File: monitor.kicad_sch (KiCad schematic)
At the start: 6 parts, among them U20 ADS8568SPM

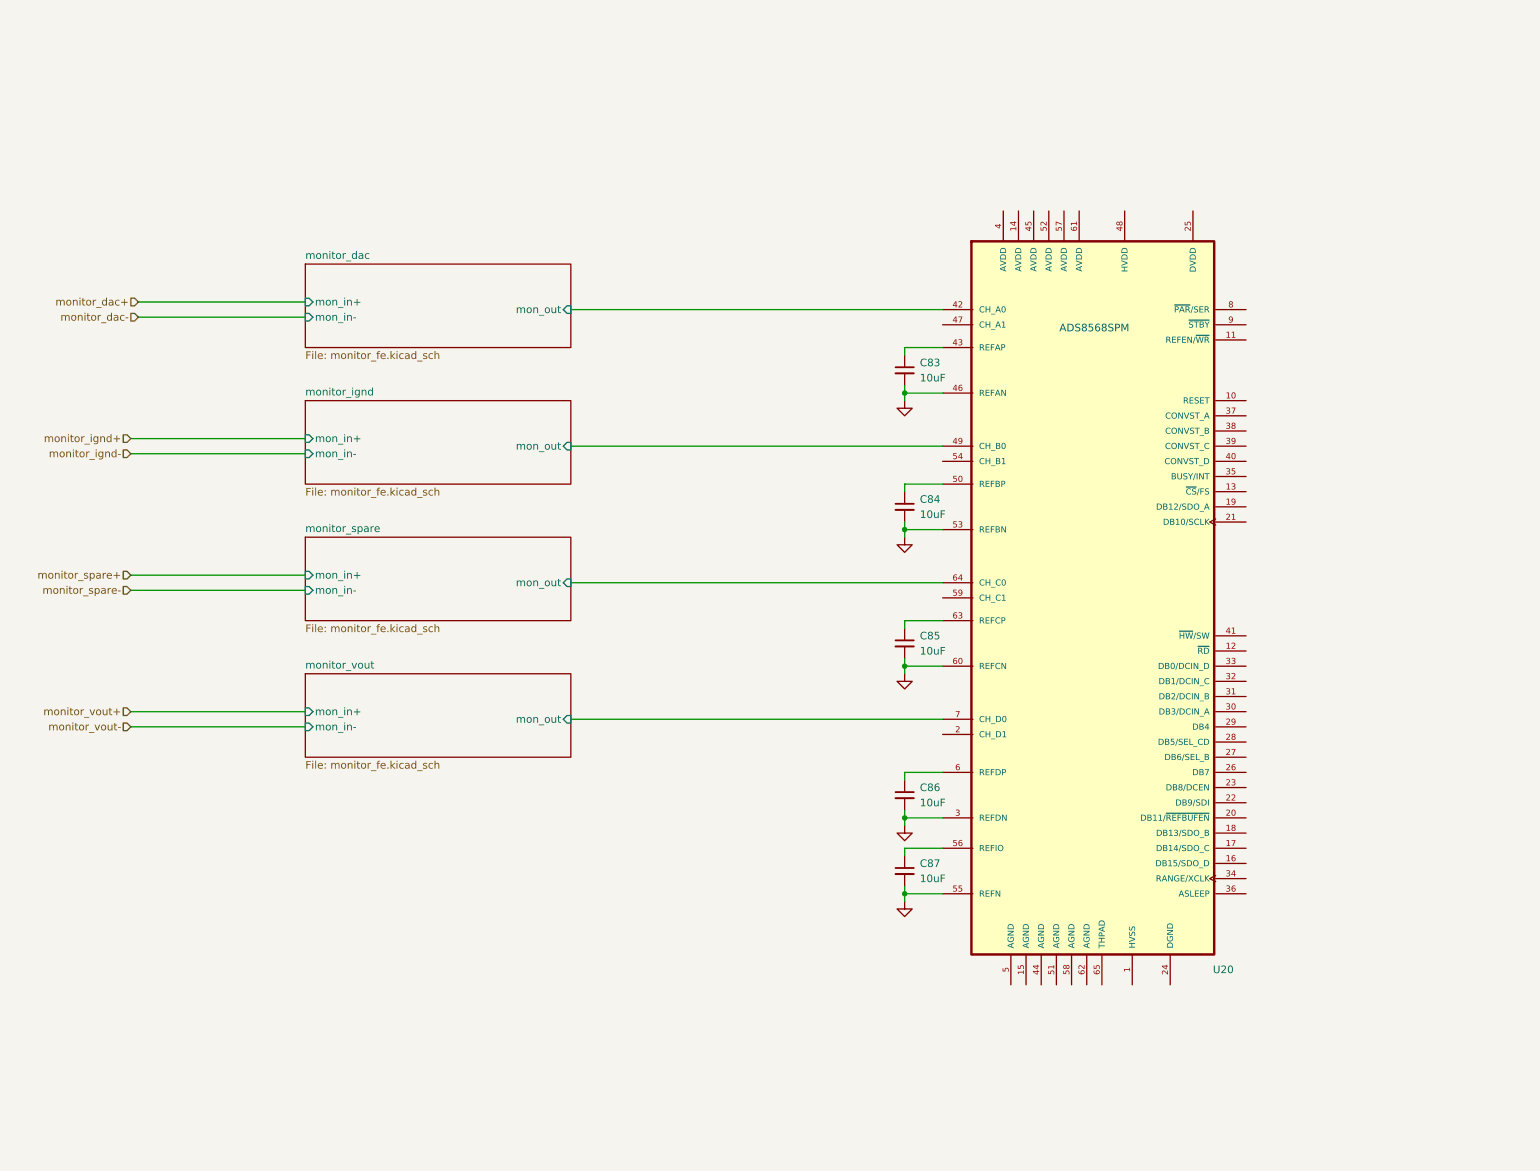
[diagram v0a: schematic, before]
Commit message: Add isolated digital I/O
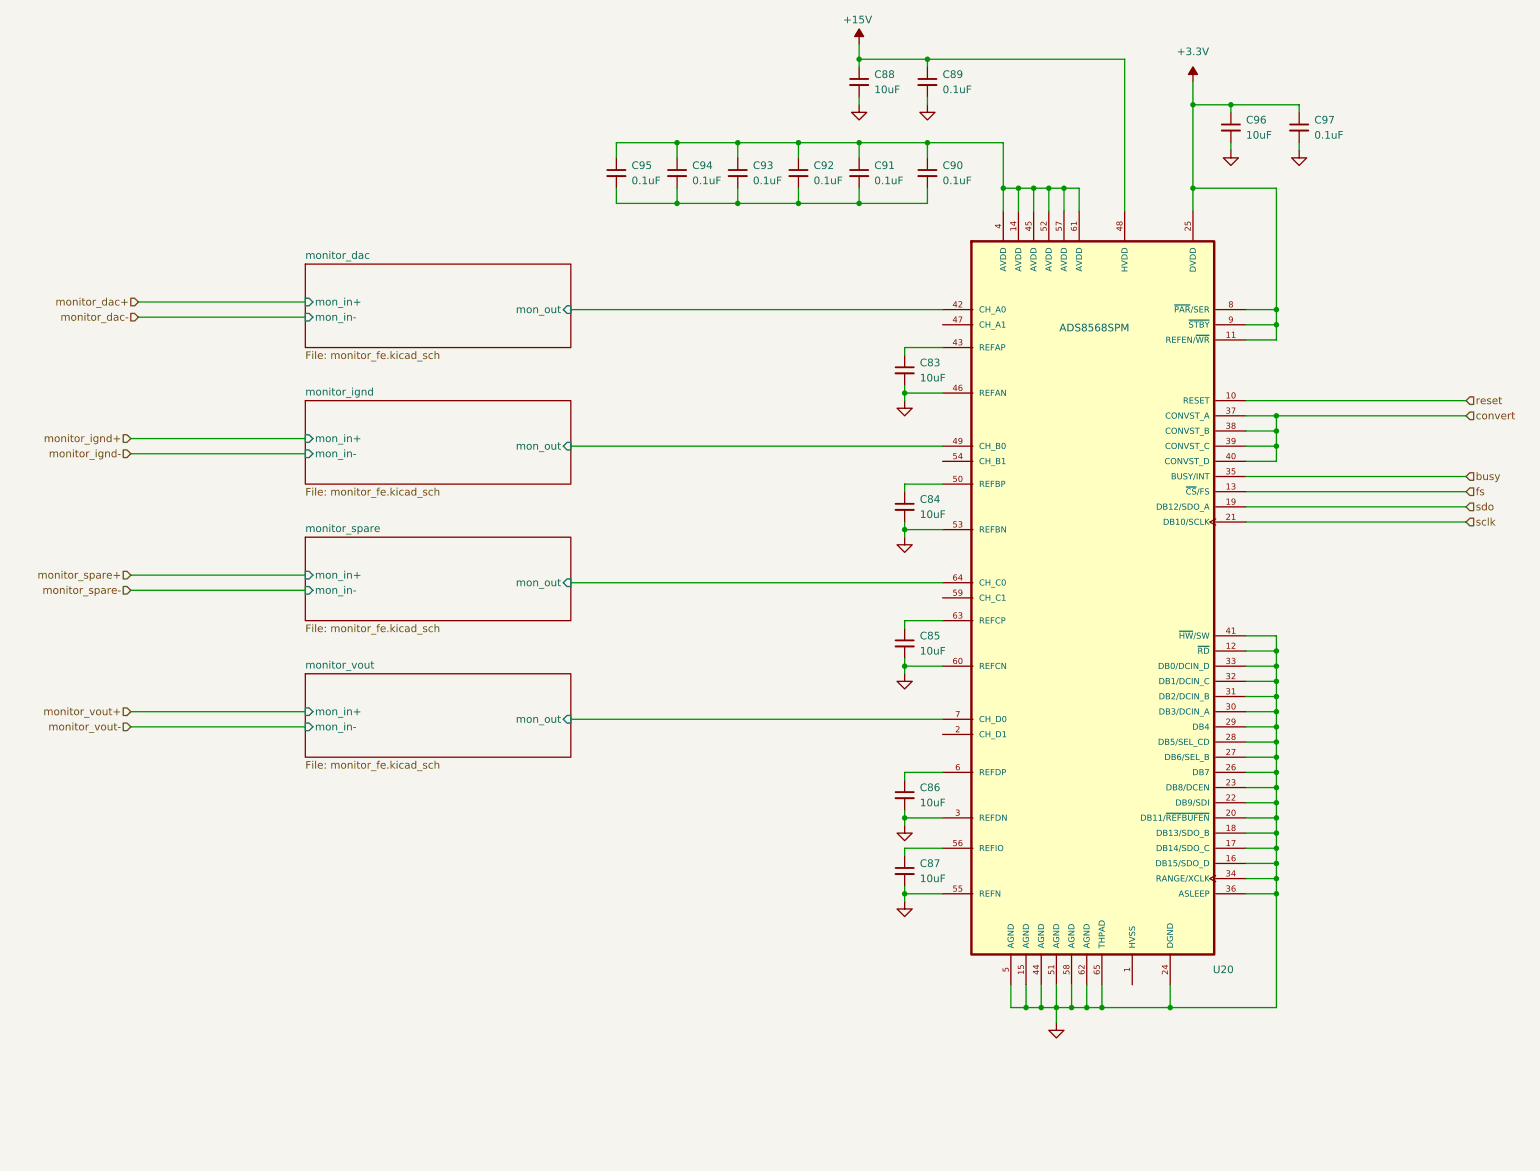
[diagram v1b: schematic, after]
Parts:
- added C88, C96: 10uF, Capacitor_SMD:C_0603_1608Metric, symbol Device:C_Small
- added C89, C90, C91, C92, C93, C94, C95, C97: 0.1uF, Capacitor_SMD:C_0402_1005Metric, symbol Device:C_Small
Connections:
- net GND: now also U20.12 (~{RD}), U20.15 (AGND), U20.16 (DB15/SDO_D), U20.17 (DB14/SDO_C), U20.18 (DB13/SDO_B), U20.20 (DB11/~{REFBUFEN}), U20.22 (DB9/SDI), U20.23 (DB8/DCEN), U20.24 (DGND), U20.26 (DB7), U20.27 (DB6/SEL_B), U20.28 (DB5/SEL_CD), U20.29 (DB4), U20.30 (DB3/DCIN_A), U20.31 (DB2/DCIN_B), U20.32 (DB1/DCIN_C), U20.33 (DB0/DCIN_D), U20.34 (RANGE/XCLK), U20.36 (ASLEEP), U20.41 (~{HW}/SW), U20.44 (AGND), U20.5 (AGND), U20.51 (AGND), U20.58 (AGND), U20.62 (AGND), U20.65 (THPAD), C88.2, C89.2, C96.2, C97.2
- net reset: now reaches U20.10 (RESET)
- net +3.3V: now reaches U20.11 (REFEN/~{WR})
- net +3.3V: now also U20.25 (DVDD), U20.8 (~{PAR}/SER), U20.9 (~{STBY}), C96.1, C97.1
- net fs: now reaches U20.13 (~{CS}/FS)
- net at U20.14 (AVDD): now also U20.4 (AVDD), U20.45 (AVDD), U20.52 (AVDD), U20.57 (AVDD), U20.61 (AVDD), C90.1, C91.1, C92.1, C93.1, C94.1, C95.1
- net sdo: now reaches U20.19 (DB12/SDO_A)
- net sclk: now reaches U20.21 (DB10/SCLK)
- net busy: now reaches U20.35 (BUSY/INT)
- net convert: now reaches U20.37 (CONVST_A)
- net convert: now also U20.38 (CONVST_B), U20.39 (CONVST_C), U20.40 (CONVST_D)
- net +15V: now reaches U20.48 (HVDD)
- net +15V: now also C88.1, C89.1
- new net: C90.2, C91.2, C92.2, C93.2, C94.2, C95.2

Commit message: Add DCCT ADCs
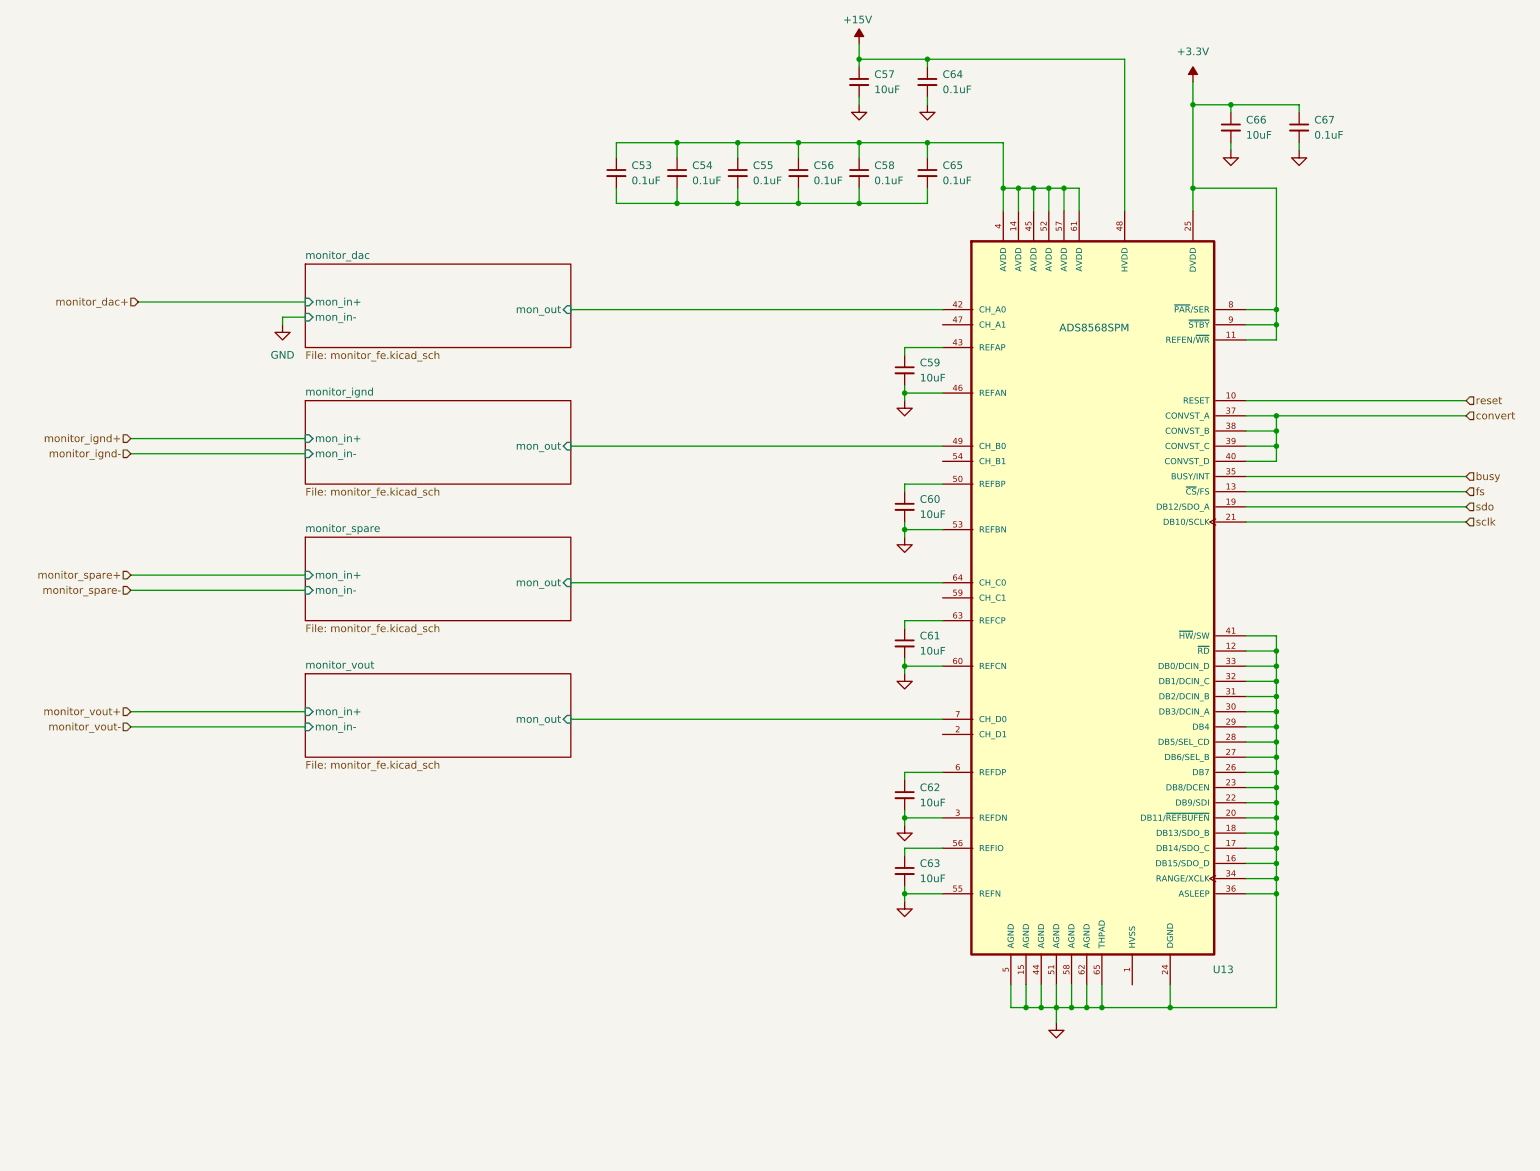
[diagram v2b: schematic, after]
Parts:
- U13: renamed from U20; footprint ADS8568SPM:QFP50P1200X1200X160-64N -> myparts:QFP50P1200X1200X160-64N
- renumbered C95 to C53, C94 to C54, C93 to C55, C92 to C56, C88 to C57, C91 to C58, C83 to C59, C84 to C60, C85 to C61, C86 to C62, C87 to C63, C89 to C64, C90 to C65, C96 to C66, C97 to C67

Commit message: DAC and DCCT placement
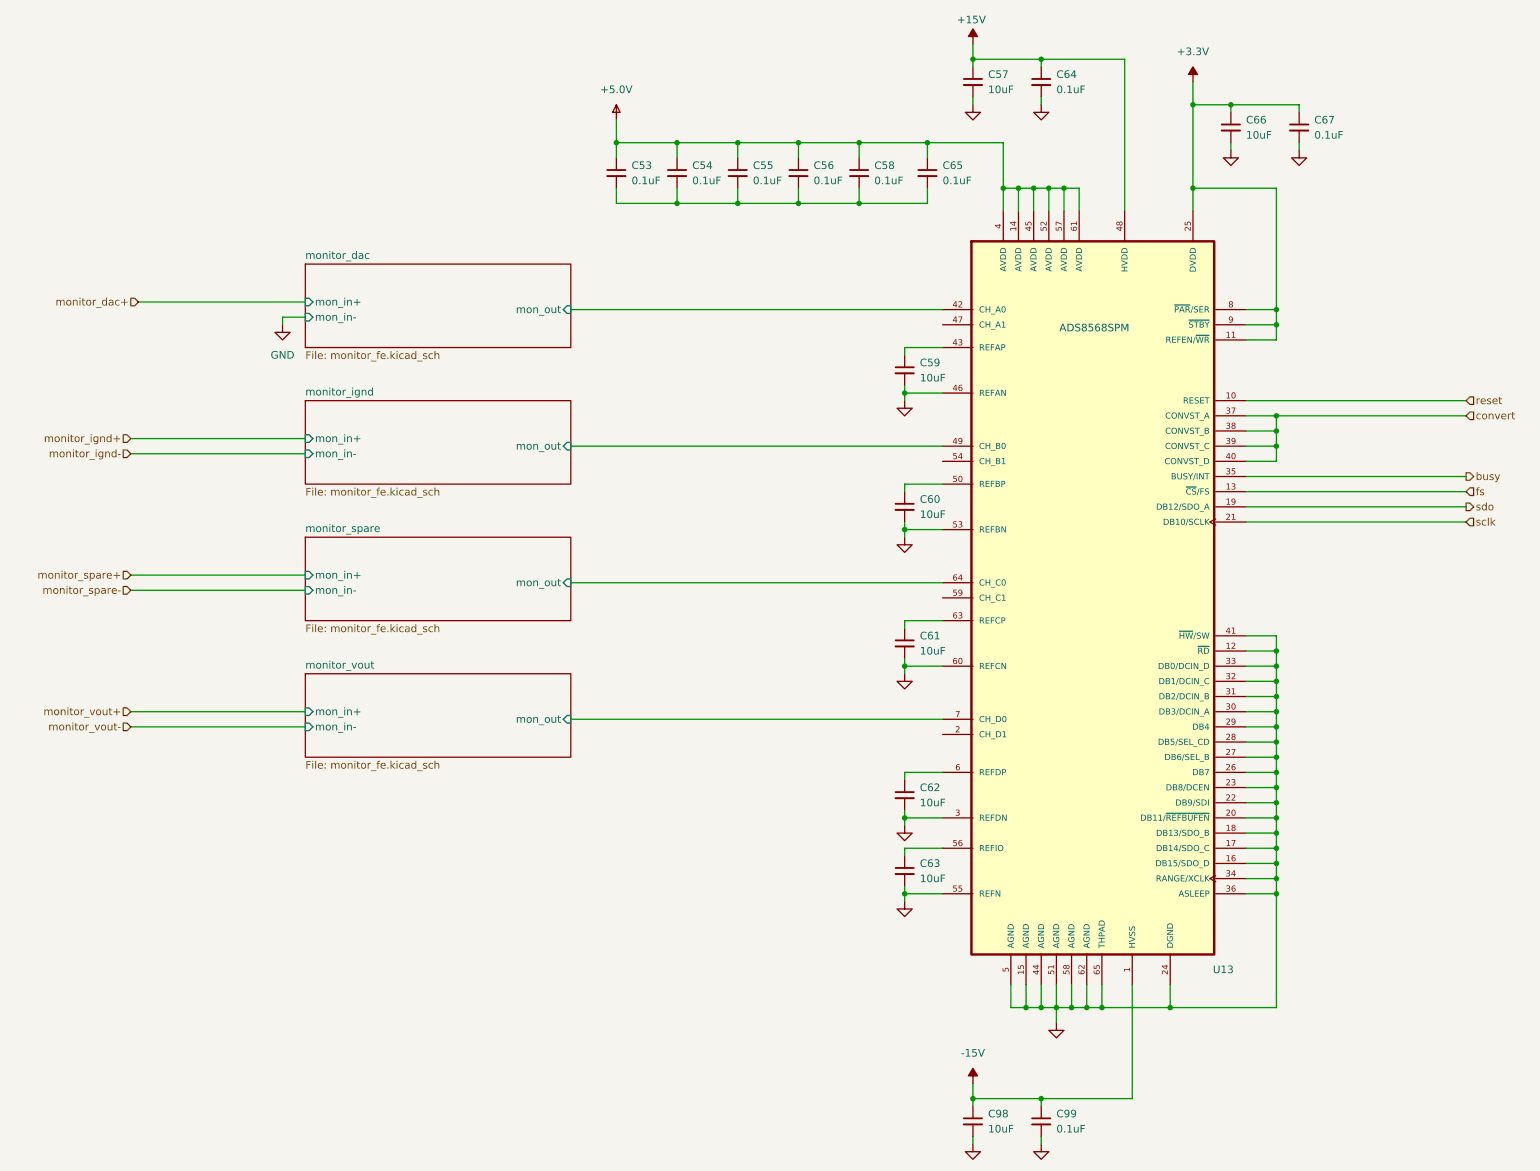
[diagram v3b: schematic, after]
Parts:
- added C98: 10uF, Capacitor_SMD:C_0603_1608Metric, symbol Device:C_Small
- added C99: 0.1uF, Capacitor_SMD:C_0402_1005Metric, symbol Device:C_Small
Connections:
- net GND: now also C98.2, C99.2
- net -15V: now reaches U13.1 (HVSS)
- net -15V: now also C98.1, C99.1
- net +5.0V: now reaches C53.1, C54.1, C55.1, C56.1, C58.1, C65.1, U13.14 (AVDD), U13.4 (AVDD), U13.45 (AVDD), U13.52 (AVDD), U13.57 (AVDD), U13.61 (AVDD)
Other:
- moved on the sheet: C57, C64

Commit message: Finish layout
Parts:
- C53, C54, C55, C56, C58, C64, C65, C67, C99: MFG (none) -> Taiyo Yuden; MFG_PN (none) -> TMK105BJ104KV-F
- C57, C59, C60, C61, C62, C63, C66, C98: MFG (none) -> Samsung; MFG_PN (none) -> CL10A106MA8NRNC
- U13: footprint myparts:QFP50P1200X1200X160-64N -> ADS8568SPM:QFP50P1200X1200X160-64N; Cost (none) -> 25.17; MFG (none) -> Analog Devices; MFG_PN (none) -> ADS8568SPM
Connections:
- net GND: now also C53.2, C54.2, C55.2, C56.2, C58.2, C65.2, U13.2 (CH_D1), U13.47 (CH_A1), U13.54 (CH_B1), U13.59 (CH_C1)
